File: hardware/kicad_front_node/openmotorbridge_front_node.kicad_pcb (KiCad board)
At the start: 4 copper layers, 82 x 50 mm, 43 parts, among them J7 USB-C_SERVICE, K1 CPC1017N_CAN_RELAY, Q1 DMN63D8_BSD_MOSFET, Q2 TPS1H100_AUX_LIGHT, SW1 BOOT, SW2 RESET, U1 ESP32-S3-WROOM-1U, U2 USB2514Bi-AEZG, U3 TPS54302_5V_BUCK, U4 TPS2051B_PORT2_GATE, U5 SW3526_USB_PD1_20W, U6 TCAN334G_CAN, U7 TLV75533P_3V3_LDO, U9 DW3110, Y1 24.000MHz

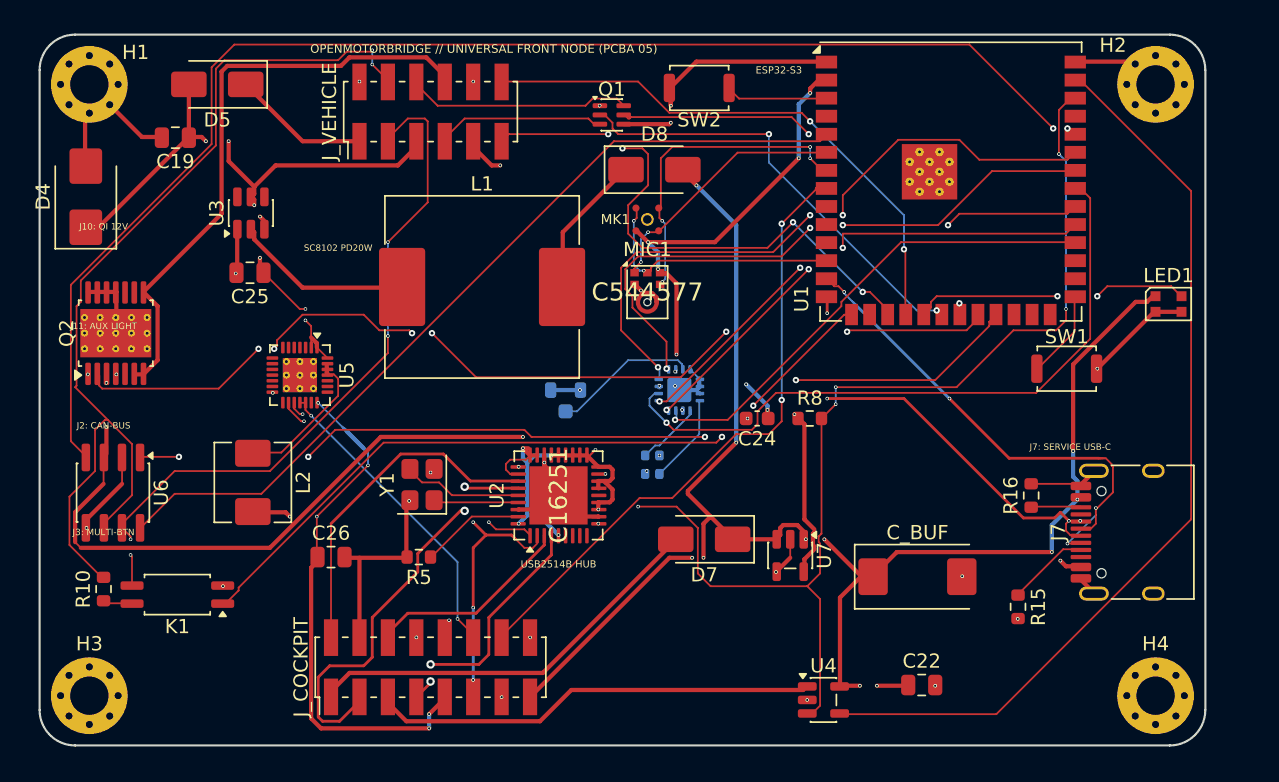
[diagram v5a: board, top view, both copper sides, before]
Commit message: feat(hw): update Front Node PCBA 05 to v10 ESP32-P4 + ESP32-E22 dual-chip architecture
- Replaced ESP32-S3 with ESP32-P4-NR16 (Dual-Core 400 MHz RISC-V, 0.0% radio on silicon, integrated 480 Mbps High-Speed USB 2.0 PHY)
- Added ESP32-E22-WROOM-2X2 companion radio (Wi-Fi 6E 5/6 GHz, 2x2 MIMO, dual U.FL ports ANT1/ANT2, connected via 4-bit SDIO 3.0)
- Eliminated 2.4 GHz radio completely from Front Node to avoid interference with Zentralbox QCC3084 / S31 Bluetooth / BLE mesh
- Removed legacy DW3110 UWB transceiver, UWB antenna, and old block pinheaders (J_VEHICLE 12P, J_COCKPIT 16P)
- Standardized all external connectors to automotive JST footprints (JST-GH, JST-SH, JST-PH) with clean unrouted layout ready for user routing
- Connected ESP32-P4 native USB HS to USB2514Bi Hub downstream port 4 for Harley Headset Emulation (MFi / UAC) and CDC-NCM Ethernet
- Routed independent USB-C service port directly to ESP32-P4 USB Serial/JTAG controller
- Updated 3D renders and documentation in docs/de/07_pcba_hardware_pinouts.md and docs/en/07_pcba_hardware_pinouts.md
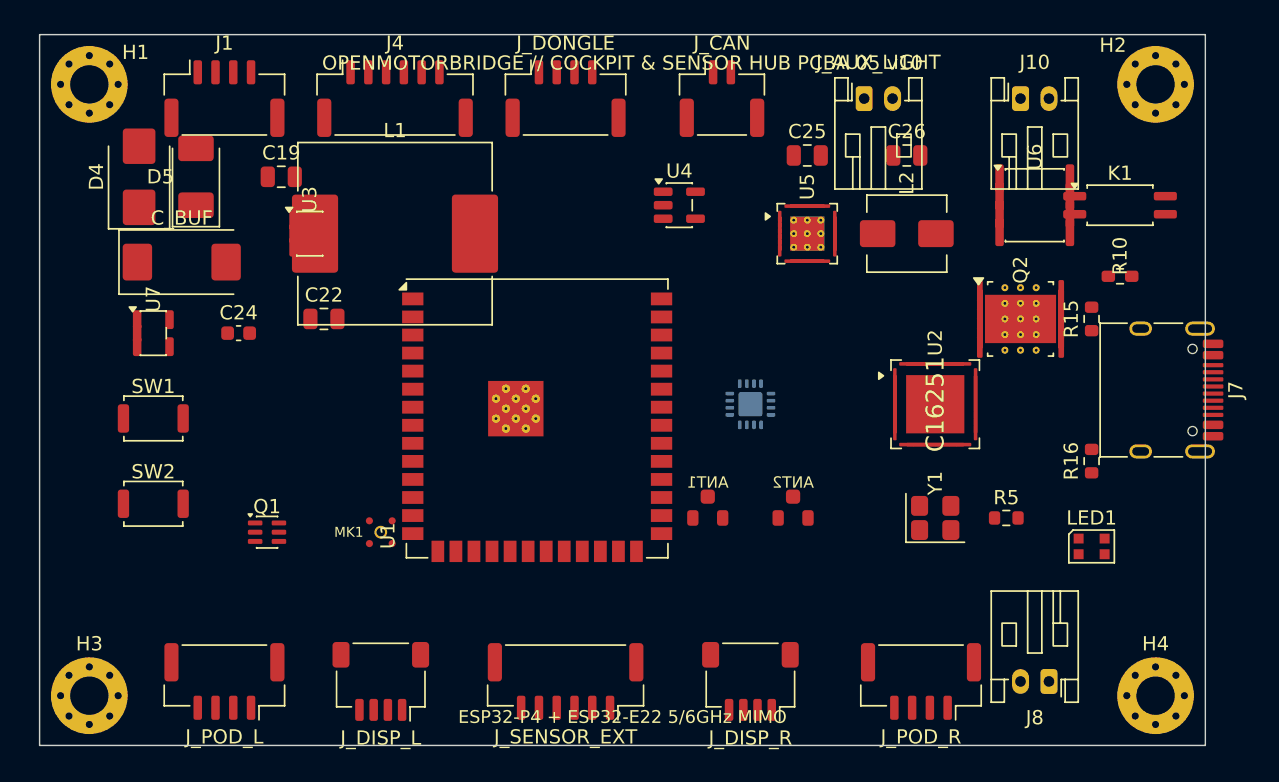
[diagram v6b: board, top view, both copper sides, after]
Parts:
- removed ANT_UWB: Taoglas_FXUWB10, Connector_Coaxial:U.FL_Hirose_U.FL-R-SMT-1_Vertical
- removed D7: SS34_USB_OR, D_SMA
- removed D8: SS34_BUCK_OR, D_SMA
- removed J_COCKPIT: COCKPIT_16P_SMD, PinHeader_2x08_P2.00mm_Vertical_SMD
- removed J_VEHICLE: VEHICLE_12P_SMD, PinHeader_2x06_P2.00mm_Vertical_SMD
- removed MIC1: MSM261S4030H0R, InvenSense_ICS-43434-6_3.5x2.65mm
- removed R8: 10k_FAULT, R_0603_1608Metric
- removed Y_UWB: 38.4MHz, Crystal:Crystal_SMD_2016-4Pin_2.0x1.6mm
- added ANT1: U.FL_5_6GHZ_MAIN, Connector_Coaxial:U.FL_Hirose_U.FL-R-SMT-1_Vertical, F.Cu at (147.0, 104.0)
- added ANT2: U.FL_5_6GHZ_MIMO, Connector_Coaxial:U.FL_Hirose_U.FL-R-SMT-1_Vertical, F.Cu at (153.0, 104.0)
- added J1: JST_GH_04P_BACKBONE, JST_GH_SM04B-GHS-TB_1x04-1MP_P1.25mm_Horizontal, F.Cu at (113.0, 74.5)
- added J10: JST_PH_02P_NAVI_PWR, JST_PH_S2B-PH-K_1x02_P2.00mm_Horizontal, F.Cu at (169.0, 74.5)
- added J4: JST_GH_06P_HUB_EXT, JST_GH_SM06B-GHS-TB_1x06-1MP_P1.25mm_Horizontal, F.Cu at (125.0, 74.5)
- added J8: JST_PH_02P_CAM_PWR, JST_PH_S2B-PH-K_1x02_P2.00mm_Horizontal, F.Cu at (171.0, 115.5)
- added J_AUX_LIGHT: JST_PH_02P_AUX_LIGHT, JST_PH_S2B-PH-K_1x02_P2.00mm_Horizontal, F.Cu at (158.0, 74.5)
- added J_CAN: JST_GH_02P_CAN, JST_GH_SM02B-GHS-TB_1x02-1MP_P1.25mm_Horizontal, F.Cu at (148.0, 74.5)
- added J_DISP_L: JST_SH_04P_DISP_L, JST_SH_SM04B-SRSS-TB_1x04-1MP_P1.00mm_Horizontal, F.Cu at (124.0, 115.5)
- added J_DISP_R: JST_SH_04P_DISP_R, JST_SH_SM04B-SRSS-TB_1x04-1MP_P1.00mm_Horizontal, F.Cu at (150.0, 115.5)
- added J_DONGLE: JST_GH_04P_DONGLE, JST_GH_SM04B-GHS-TB_1x04-1MP_P1.25mm_Horizontal, F.Cu at (137.0, 74.5)
- added J_POD_L: JST_GH_04P_POD_L, JST_GH_SM04B-GHS-TB_1x04-1MP_P1.25mm_Horizontal, F.Cu at (113.0, 115.5)
- added J_POD_R: JST_GH_04P_POD_R, JST_GH_SM04B-GHS-TB_1x04-1MP_P1.25mm_Horizontal, F.Cu at (162.0, 115.5)
- added J_SENSOR_EXT: JST_GH_06P_SENSOR_PUCK, JST_GH_SM06B-GHS-TB_1x06-1MP_P1.25mm_Horizontal, F.Cu at (137.0, 115.5)
- C_BUF: value 470uF_10V_POLYMER -> 470uF_25V_POLYMER
- J7: value USB-C_SERVICE -> USB_C_SERVICE
- U1: value ESP32-S3-WROOM-1U -> ESP32-P4-NR16
- U5: value SW3526_USB_PD1_20W -> SW3526_USB_PD1_30W
- U9: value DW3110 -> ESP32-E22-WROOM-2X2
- moved R10 74.8 mm to (176.0, 87.0), turned to 0 degrees
- moved K1 71.7 mm to (176.0, 82.0), turned to 0 degrees
- moved U6 67.9 mm to (170.0, 82.0), turned to 0 degrees
- moved SW1 64.3 mm to (108.0, 97.0)
- moved Q2 63.6 mm to (169.0, 90.0), turned to 0 degrees
- moved C_BUF 56.3 mm to (110.0, 86.0)
- moved C26 49.4 mm to (161.0, 78.5)
- moved C22 49.3 mm to (120.0, 90.0)
- moved L2 49.2 mm to (161.0, 84.0), turned to 0 degrees
- moved SW2 48.3 mm to (108.0, 103.0), turned to 0 degrees
- moved U7 47.5 mm to (108.0, 91.0), turned to 0 degrees
- moved R5 41.4 mm to (168.0, 104.0), turned to 0 degrees
- moved C25 40.1 mm to (154.0, 78.5), turned to 0 degrees
- moved Q1 38.1 mm to (116.0, 105.0)
- moved U5 37.0 mm to (154.0, 84.0), turned to 0 degrees
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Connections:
- Q2 pad 5: (no net) -> GND
- U1 pad 24: (no net) -> USB_SERV_DM
- U1 pad 25: (no net) -> USB_SERV_DP
- U1 pad 37: (no net) -> E22_IRQ
- U2 pad 14: (no net) -> GND
- U3 pad 4: (no net) -> VCC_5V
- U3 pad 6: (no net) -> SW_BUCK
- U5 pad 3: (no net) -> VBUS_PD1_OUT
- U5 pad 4: (no net) -> GND
- U5 pad 5: (no net) -> USB_DN1_CC1
- U5 pad 6: (no net) -> USB_DN1_CC2
- U5 pad 7: (no net) -> USB_DN1_DP
- U5 pad 8: (no net) -> USB_DN1_DM
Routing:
- net VCC_3V3: track 154.2 -> 0.00 mm, vias 20 -> 0
- net VCC_5V: track 113.4 -> 0.00 mm, vias 12 -> 0
- net TWAI_RX: track 96.0 -> 0.00 mm, vias 2 -> 0
- net GND: track 95.5 -> 0.00 mm, vias 32 -> 0
- net OTTOCAST_FAULT_N: track 79.4 -> 0.00 mm, vias 6 -> 0
- net AUX_LIGHT_EN: track 69.0 -> 0.00 mm, vias 6 -> 0
- net CAN_L: track 66.5 -> 0.00 mm, vias 2 -> 0
- net OTTOCAST_PWR_EN: track 65.0 -> 0.00 mm
- net TWAI_TX: track 65.0 -> 0.00 mm, vias 4 -> 0
- net +12V_PROT: track 62.7 -> 0.00 mm, vias 7 -> 0
- net CAN_SILENT: track 59.9 -> 0.00 mm
- net CAN_TERM_EN: track 52.8 -> 0.00 mm, vias 2 -> 0
- net CAN_H: track 49.5 -> 0.00 mm, vias 4 -> 0
- net UWB_CS: track 47.7 -> 0.00 mm, vias 1 -> 0
- net UWB_RST: track 46.3 -> 0.00 mm, vias 3 -> 0
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- removed copper zone on In1.Cu, net GND
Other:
- outline, holes or cut-outs redrawn
- board text added: "ESP32-P4 + ESP32-E22 5/6GHz MIMO"
- board text added: "OPENMOTORBRIDGE // COCKPIT & SENSOR HUB PCBA 05 v10"
- board text removed: "ESP32-S3"
- board text removed: "J10: QI 12V"
- board text removed: "J11: AUX LIGHT"
- board text removed: "J2: CAN-BUS"
- board text removed: "J3: MULTI-BTN"
- board text removed: "J7: SERVICE USB-C"
- board text removed: "OPENMOTORBRIDGE // UNIVERSAL FRONT NODE (PCBA 05)"
- board text removed: "SC8102 PD20W"
- board text removed: "USB2514B HUB"

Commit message: hardware(front-node): connect all nets in schematic and PCB with passives parity
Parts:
- removed J7: USB_C_SERVICE, USB_C_Receptacle_HRO_TYPE-C-31-M-12
- removed J_CAN: JST_GH_02P_CAN, JST_GH_SM02B-GHS-TB_1x02-1MP_P1.25mm_Horizontal
- removed K1: CPC1017N_CAN_RELAY, SOP-4_4.4x2.6mm_P1.27mm
- removed R10: 120R_CAN, R_0603_1608Metric
- removed R15: 5.1k_CC1, R_0603_1608Metric
- removed R16: 5.1k_CC2, R_0603_1608Metric
- removed U6: TCAN334G_CAN, SOIC-8_3.9x4.9mm_P1.27mm
- added C_BOOT: 100nF, Capacitor_SMD:C_0603_1608Metric, F.Cu at (171.0, 85.0)
- added C_EN: 1uF, Capacitor_SMD:C_0603_1608Metric, F.Cu at (105.0, 104.5)
- added C_LED: 100nF, Capacitor_SMD:C_0603_1608Metric, F.Cu at (178.5, 104.0)
- added C_MIC: 100nF, Capacitor_SMD:C_0603_1608Metric, F.Cu at (108.5, 113.5)
- added C_VDD18: 1uF, Capacitor_SMD:C_0603_1608Metric, F.Cu at (128.9, 98.0)
- added C_XTAL1: 18pF, Capacitor_SMD:C_0603_1608Metric, F.Cu at (126.5, 104.5)
- added C_XTAL2: 18pF, Capacitor_SMD:C_0603_1608Metric, F.Cu at (131.5, 104.5)
- added R_BOOT: 10k, Resistor_SMD:R_0603_1608Metric, F.Cu at (103.0, 85.5)
- added R_BTN_L: 10k, Resistor_SMD:R_0603_1608Metric, F.Cu at (167.5, 110.5)
- added R_BTN_R: 10k, Resistor_SMD:R_0603_1608Metric, F.Cu at (117.5, 110.5)
- added R_E22_EN: 10k, Resistor_SMD:R_0603_1608Metric, F.Cu at (114.5, 76.5)
- added R_EN: 10k, Resistor_SMD:R_0603_1608Metric, F.Cu at (103.0, 104.5)
- added R_FB1: 100k, Resistor_SMD:R_0603_1608Metric, F.Cu at (173.5, 85.0)
- added R_FB2: 13.7k, Resistor_SMD:R_0603_1608Metric, F.Cu at (173.5, 87.0)
- added R_HUB_RST: 10k, Resistor_SMD:R_0603_1608Metric, F.Cu at (132.5, 98.0)
- added R_SCL: 4.7k, Resistor_SMD:R_0603_1608Metric, F.Cu at (141.5, 111.5)
- added R_SDA: 4.7k, Resistor_SMD:R_0603_1608Metric, F.Cu at (141.5, 109.5)
- added R_SDIO_CMD: 10k, Resistor_SMD:R_0603_1608Metric, F.Cu at (116.5, 76.5)
- added R_SDIO_D0: 10k, Resistor_SMD:R_0603_1608Metric, F.Cu at (114.5, 78.5)
- added R_SDIO_D1: 10k, Resistor_SMD:R_0603_1608Metric, F.Cu at (116.5, 78.5)
- added R_SDIO_D2: 10k, Resistor_SMD:R_0603_1608Metric, F.Cu at (114.5, 80.5)
- added R_SDIO_D3: 10k, Resistor_SMD:R_0603_1608Metric, F.Cu at (116.5, 80.5)
- D4, D5, U2, Y1: moved to B.Cu
- U9: moved to F.Cu
- moved C_BUF 69.4 mm to (179.2, 81.5), turned to 90 degrees
- moved J_POD_L 57.5 mm to (170.5, 116.5), turned to 0 degrees
- moved ANT2 54.8 mm to (108.5, 72.0), turned to 180 degrees
- moved U3 53.7 mm to (172.6, 81.8)
- moved L1 51.3 mm to (175.0, 95.5), turned to -90 degrees
- moved ANT1 47.3 mm to (112.2, 72.0), turned to 180 degrees
- moved U9 44.1 mm to (110.0, 77.2), turned to 90 degrees
- moved C19 42.6 mm to (159.1, 87.0), turned to 180 degrees
- moved J_POD_R 40.5 mm to (121.5, 116.5), turned to 0 degrees
- moved J8 38.6 mm to (170.2, 77.0)
- moved J_DISP_L 35.5 mm to (159.5, 116.5), turned to 0 degrees
- moved U2 34.3 mm to (128.9, 92.0), turned to 90 degrees
- moved Y1 33.9 mm to (129.1, 102.9), turned to 180 degrees
- moved Q1 29.9 mm to (145.6, 108.9), turned to -90 degrees
- moved C24 27.2 mm to (133.5, 110.0)
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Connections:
- ANT1 pad 1: UWB_RF -> E22_RF_MAIN
- ANT2 pad 1: UWB_RF -> E22_RF_MIMO
- C_BUF pad 1: VCC_5V -> +12V_PROT
- D4 pad 1: +12V_PROT -> VIN_60W
- D5 pad 1: KL15_12V_SW -> VIN_60W
- L1 pad 2: VBUS_BUCK_OUT -> VCC_5V
- LED1 pad 1: VCC_5V -> (no net)
- LED1 pad 2: GND -> WS2812B_DIN
- LED1 pad 3: GND -> VCC_5V
- LED1 pad 4: WS2812B_DIN -> GND
- MK1 pad 4: VCC_3V3 -> GND
- Q1 pad 3: BSD_RIGHT_N -> BSD_LED_R_N
- Q1 pad 6: BSD_LEFT_N -> BSD_LED_L_N
- Q2 pad 11: +12V_PROT -> (no net)
- Q2 pad 12: +12V_PROT -> (no net)
- Q2 pad 13: +12V_PROT -> (no net)
- Q2 pad 14: +12V_PROT -> (no net)
- Q2 pad 15: +12V_PROT -> GND
- Q2 pad 3: VCC_3V3 -> +12V_PROT
- Q2 pad 4: GND -> +12V_AUX
- Q2 pad 6: +12V_AUX -> (no net)
- Q2 pad 7: +12V_AUX -> (no net)
- Q2 pad 8: +12V_AUX -> (no net)
- U1 pad 10: PTT_IN3_N -> (no net)
- U1 pad 13: USB_SERV_DM -> USB_HS_DM
- U1 pad 14: USB_SERV_DP -> USB_HS_DP
- U1 pad 15: CAN_TERM_EN -> (no net)
- U1 pad 23: TWAI_TX -> (no net)
- U1 pad 24: USB_SERV_DM -> (no net)
- U1 pad 25: USB_SERV_DP -> (no net)
- U1 pad 30: UWB_SCK -> SDIO_CLK
- U1 pad 31: UWB_MOSI -> SDIO_CMD
- U1 pad 32: UWB_MISO -> SDIO_D0
- U1 pad 33: UWB_CS -> SDIO_D1
- U1 pad 34: UWB_IRQ -> SDIO_D2
- U1 pad 35: UWB_RST -> SDIO_D3
- U1 pad 36: TWAI_RX -> (no net)
- U1 pad 38: OTTOCAST_FAULT_N -> CP2AA_FAULT_N
- U1 pad 39: OTTOCAST_PWR_EN -> CP2AA_PWR_EN
- U1 pad 40: GND -> E22_EN
- U1 pad 5: CAN_SILENT -> (no net)
- U1 pad 8: PTT_IN1_N -> BTN_SIG_L_N
- U1 pad 9: PTT_IN2_N -> BTN_SIG_R_N
- U2 pad 11: GND -> VCC_3V3
- U2 pad 12: VCC_3V3 -> XTAL_IN
- U2 pad 13: VCC_3V3 -> XTAL_OUT
- U2 pad 17: OTTOCAST_FAULT_N -> VCC_3V3
- U2 pad 20: VCC_3V3 -> USB_UP_DM
- U2 pad 21: VCC_3V3 -> USB_UP_DP
- U2 pad 23: VCC_3V3 -> GND
- U2 pad 24: VCC_3V3 -> VCC_5V
- U2 pad 26: VCC_3V3 -> GND
- U2 pad 27: VCC_3V3 -> GND
- U2 pad 30: USB_UP_DM -> VCC_3V3
- U2 pad 31: USB_UP_DP -> VDD18_CORE
- U2 pad 32: XTAL_OUT -> VCC_3V3
- U2 pad 33: XTAL_IN -> HUB_RESET_N
- U2 pad 35: HUB_RBIAS -> VCC_3V3
- U2 pad 36: VCC_3V3 -> HUB_RBIAS
- U2 pad 8: USB_DN4_DM -> USB_HS_DM
- U2 pad 9: USB_DN4_DP -> USB_HS_DP
- U3 pad 4: VCC_5V -> FB_5V
- U3 pad 6: SW_BUCK -> BOOT_5V
- U4 pad 1: VCC_5V_OTTOCAST -> VCC_5V
- U4 pad 3: OTTOCAST_FAULT_N -> CP2AA_PWR_EN
- U4 pad 4: OTTOCAST_PWR_EN -> CP2AA_FAULT_N
- U4 pad 5: VCC_5V -> VCC_5V_DONGLE
- U5 pad 14: GND -> (no net)
- U5 pad 16: USB_DN1_DP -> (no net)
- U5 pad 17: USB_DN1_DM -> (no net)
- U5 pad 18: USB_DN1_CC -> (no net)
- U5 pad 19: USB_DN1_CC -> (no net)
- U5 pad 2: +12V_PROT -> SW_PD1_BUCK
- U5 pad 21: VBUS_PD1_OUT -> (no net)
- U5 pad 25: SW_PD1_BUCK -> (no net)
- U5 pad 26: SW_PD1_BUCK -> (no net)
- U5 pad 27: SW_PD1_BUCK -> (no net)
- U5 pad 28: +12V_PROT -> (no net)
- U7 pad 4: GND -> (no net)
- U9 pad 1: GND -> VCC_3V3
- U9 pad 10: UWB_CS -> E22_IRQ
- U9 pad 11: GND -> E22_RF_MAIN
- U9 pad 12: UWB_RST -> E22_RF_MIMO
- U9 pad 13: UWB_IRQ -> GND
- U9 pad 14: VCC_3V3 -> GND
- U9 pad 15: UWB_RF -> GND
- U9 pad 3: GND -> E22_EN
- U9 pad 4: UWB_XTAL1 -> SDIO_CLK
- U9 pad 5: UWB_XTAL2 -> SDIO_CMD
- U9 pad 6: GND -> SDIO_D0
- U9 pad 7: UWB_SCK -> SDIO_D1
- U9 pad 8: UWB_MISO -> SDIO_D2
- U9 pad 9: UWB_MOSI -> SDIO_D3
